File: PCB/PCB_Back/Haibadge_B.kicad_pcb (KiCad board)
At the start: 2 copper layers, 79.8 x 79.8 mm, 76 parts, among them J1 Sensor connector, J2 USB_C_Receptacle_USB2.0, J3 Lipo connector, Q1 UMH3N, Q3 Q_PMOS_GSD, SW1 SW_Push_Dual, SW2 SW_PWR, U1 ESP-12E, U2 CH340C, U3 MCP73831-2-OT, U4 MCP1700x-330xxTT, U6 BME680

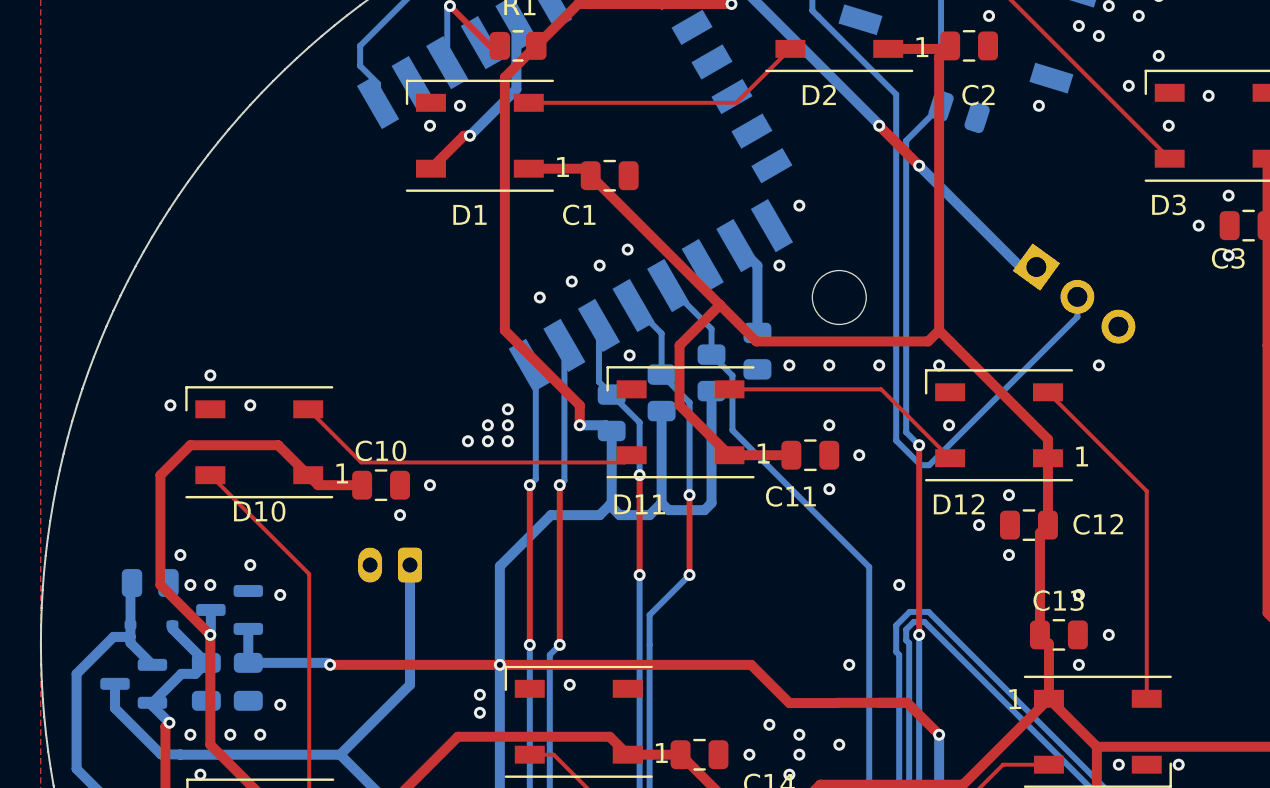
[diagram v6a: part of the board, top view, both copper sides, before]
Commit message: Added R14 10k Pullup to GPIO2
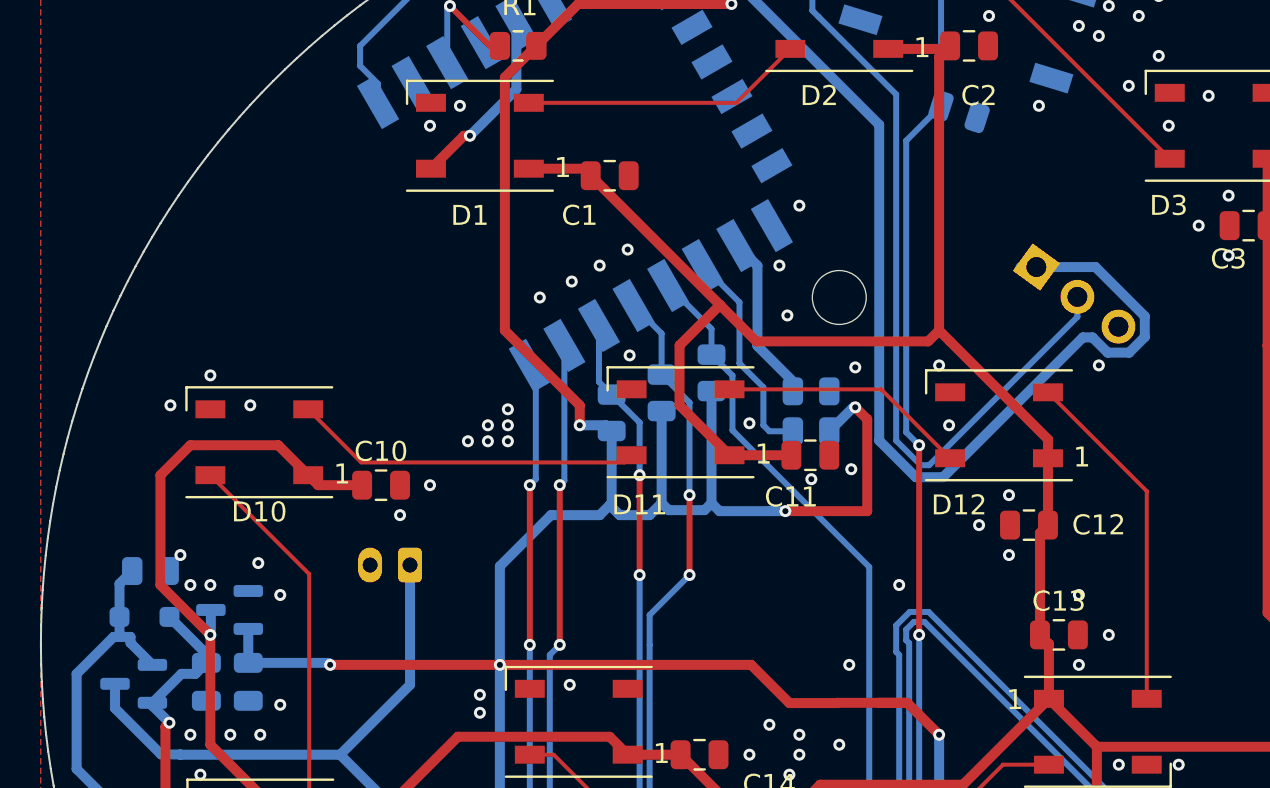
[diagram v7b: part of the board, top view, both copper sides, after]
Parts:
- added R14: 10k, Resistor_SMD:R_0805_2012Metric, B.Cu at (138.6, 129.3)
- D17: footprint Diode_SMD:D_SOD-323 -> Diode_SMD:D_SOD-323_HandSoldering
- moved R2 3.36 mm to (138.6, 127.3), turned to 0 degrees
- moved R13 0.60 mm to (105.5, 136.3)
- moved D17 0.53 mm to (105.2, 138.6)
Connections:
- U1 pad 17: unconnected-(U1-GPIO2-Pad17) -> Net-(U1-GPIO2)
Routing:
- net +3V3: track 211.6 -> 257.7 mm
- net Net-(U1-GPIO2): track 0.00 -> 10.9 mm
- net Net-(U1-GPIO15): track 4.79 -> 7.95 mm
- net +5V: track 74.7 -> 75.5 mm
- net GND: vias 135 -> 134

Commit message: Switched D16 Resistor from 1k to 2k
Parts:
- R4: value 1k -> 2k
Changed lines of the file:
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@@
 		(tags "resistor")
 		(property "Reference" "R4"
-			(at 0 1.65 0)
+			(at 0 2.05 0)
 			(layer "B.SilkS")
 			(effects
@@
 			)
 		)
-		(property "Value" "1k"
+		(property "Value" "2k"
 			(at 0 -1.65 0)
 			(layer "B.Fab")
@@
 		)
 		(property "Value" "LED"
-			(at 0 -1.82 0)
+			(at 0.05 3.5 0)
 			(layer "B.Fab")
 			(effects
